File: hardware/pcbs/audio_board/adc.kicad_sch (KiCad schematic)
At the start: 13 parts, among them U3 TAA3040

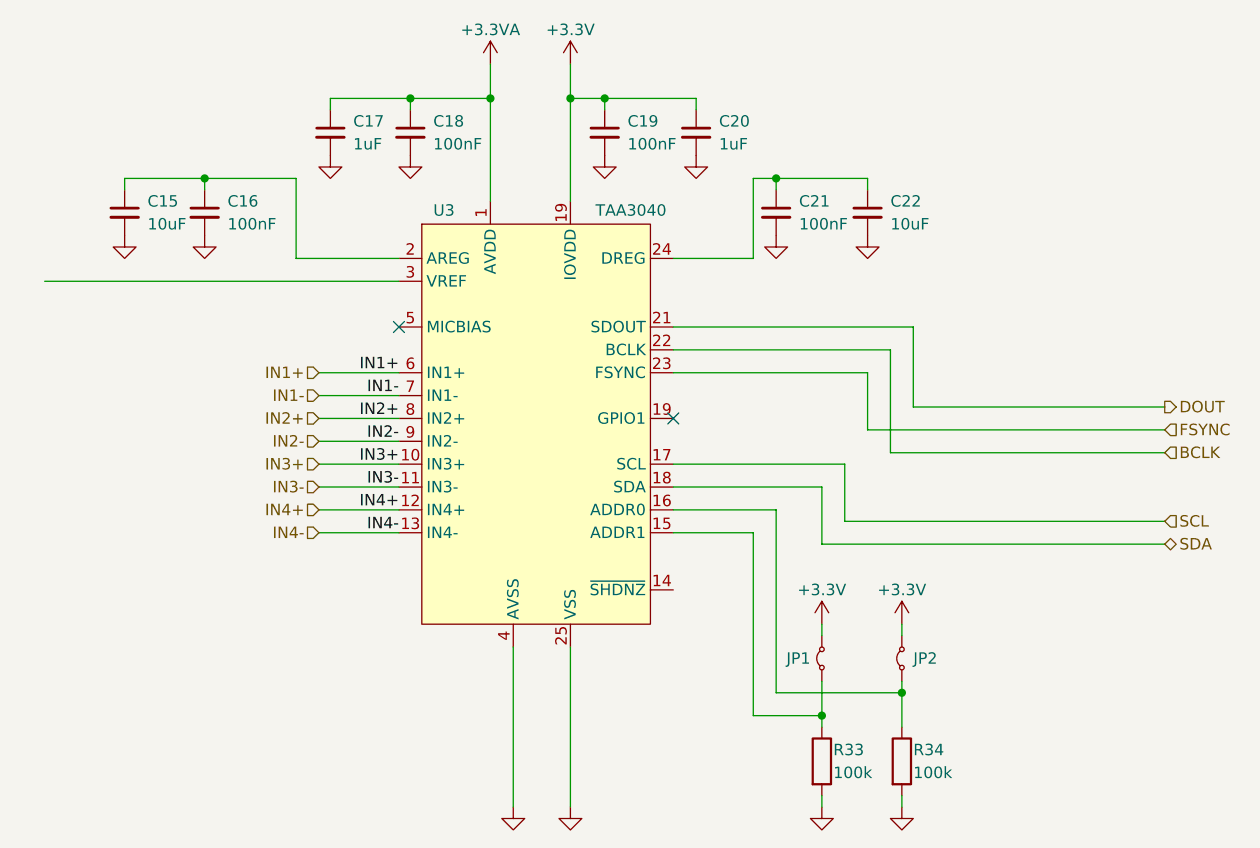
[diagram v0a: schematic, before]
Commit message: All parts placed
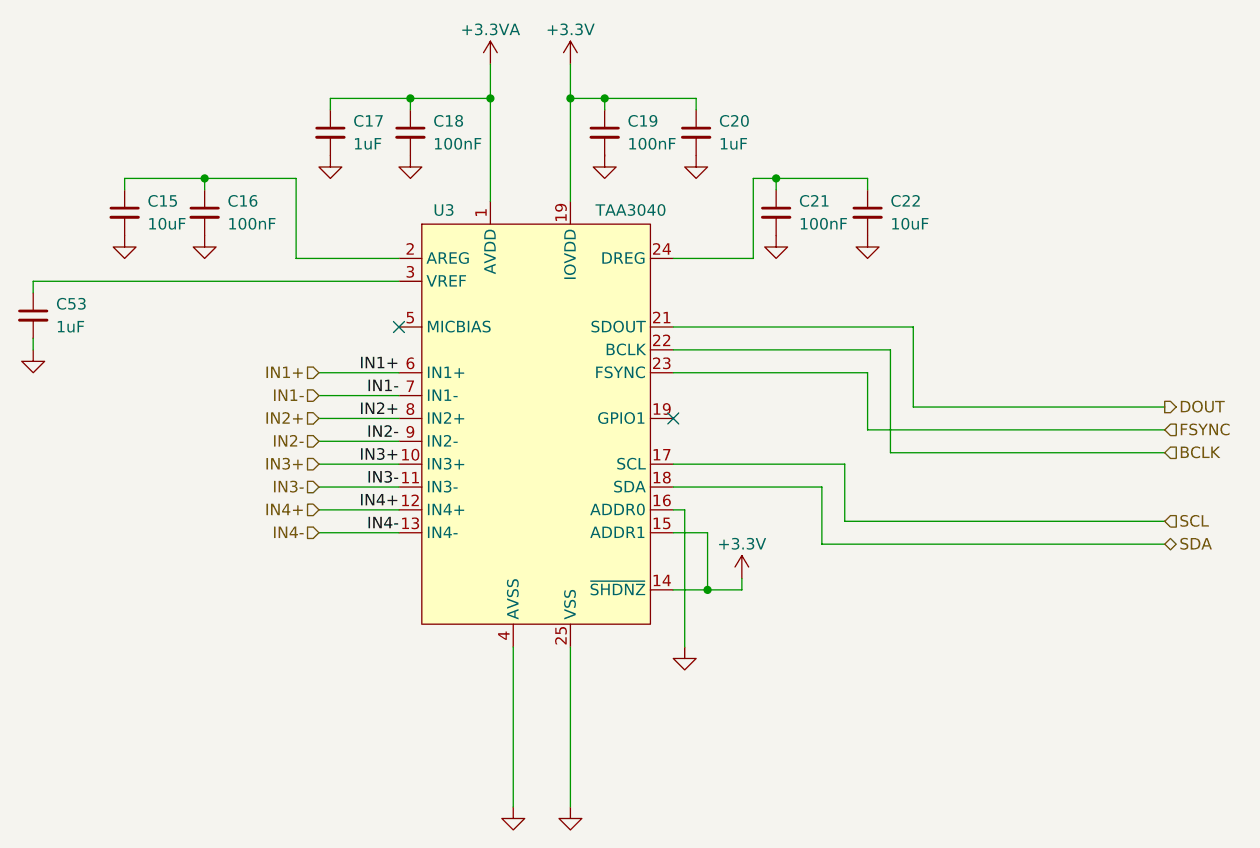
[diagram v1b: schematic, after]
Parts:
- removed JP1, JP2: Jumper_2_Small_Bridged, symbol Jumper:Jumper_2_Small_Bridged
- removed R33, R34: 100k, Resistor_SMD:R_0805_2012Metric, symbol Device:R
- added C53: 1uF, Capacitor_SMD:C_0805_2012Metric, symbol Device:C_Small
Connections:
- net +3.3V: now also U3.14 (~{SHDNZ}), U3.15 (ADDR1)
- net GND: now also U3.16 (ADDR0), C53.2
- net at U3.3 (VREF): now also C53.1
